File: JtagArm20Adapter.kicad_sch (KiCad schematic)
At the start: 7 parts, among them J1 Conn_02x03_Odd_Even, J2 Conn_01x05, J3 Conn_01x03, J4 Conn_02x10_Odd_Even, J5 B3B-PH-SM4-TB_LF__SN_

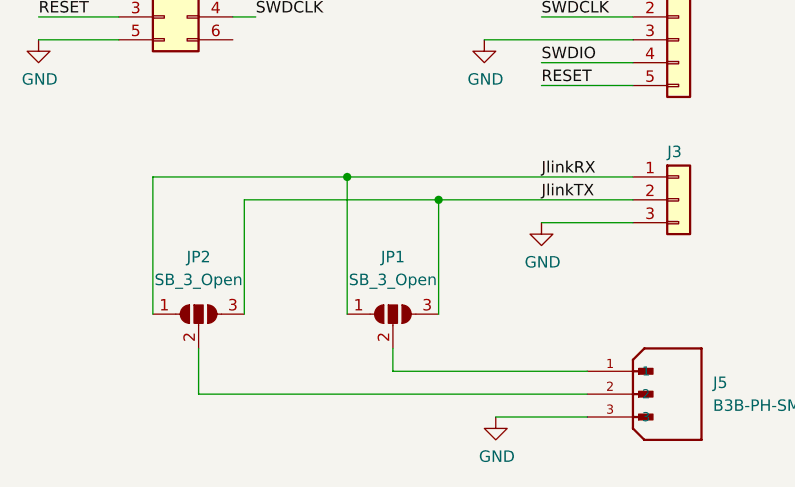
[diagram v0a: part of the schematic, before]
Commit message: moving solder bridges to top layer
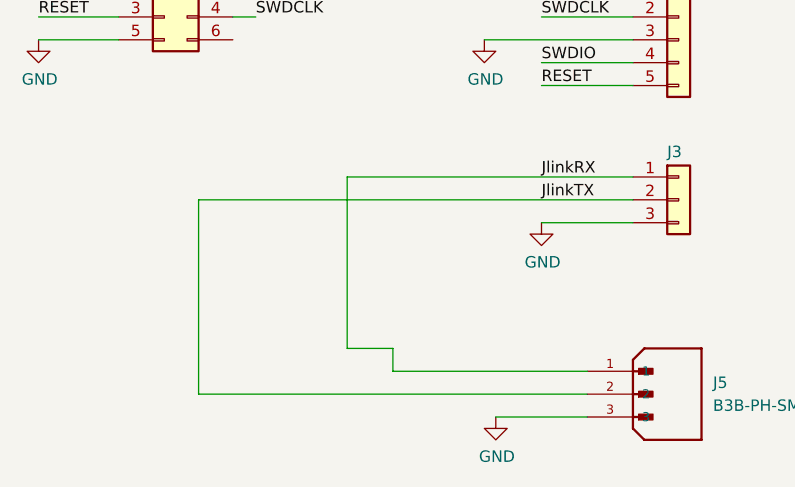
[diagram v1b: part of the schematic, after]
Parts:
- removed JP1, JP2: SB_3_Open, Jumper:SolderJumper-3_P1.3mm_Open_RoundedPad1.0x1.5mm, symbol Jumper:SolderJumper_3_Open
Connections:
- net JlinkRX: now also J5.1
- net JlinkTX: now also J5.2
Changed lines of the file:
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@@
-	)
-	(junction
-		(at 134.62 86.36)
-		(diameter 0)
-		(color 0 0 0 0)
 	)
 	(junction
@@
 	)
 	(junction
-		(at 124.46 83.82)
-		(diameter 0)
-		(color 0 0 0 0)
-	)
-	(junction
 		(at 237.49 71.12)
 		(diameter 0)
@@
 	(wire
 		(pts
-			(xy 134.62 99.06) (xy 134.62 86.36)
+			(xy 107.95 86.36) (xy 156.21 86.36)
 		)
 		(stroke
@@
 	(wire
 		(pts
-			(xy 102.87 99.06) (xy 102.87 83.82)
-		)
-		(stroke
-			(width 0)
-			(type default)
-		)
-	)
-	(wire
-		(pts
-			(xy 102.87 83.82) (xy 124.46 83.82)
-		)
-		(stroke
-			(width 0)
-			(type default)
-		)
-	)
-	(wire
-		(pts
 			(xy 237.49 71.12) (xy 237.49 83.82)
 		)
@@
 	(wire
 		(pts
-			(xy 107.95 102.87) (xy 107.95 107.95)
-		)
-		(stroke
-			(width 0)
-			(type default)
-		)
-	)
-	(wire
-		(pts
 			(xy 196.85 58.42) (xy 213.36 58.42)
 		)
@@
 	(wire
 		(pts
+			(xy 107.95 86.36) (xy 107.95 107.95)
+		)
+		(stroke
+			(width 0)
+			(type default)
+		)
+	)
+	(wire
+		(pts
 			(xy 146.05 71.12) (xy 156.21 71.12)
 		)
@@
 	(wire
 		(pts
-			(xy 124.46 99.06) (xy 124.46 83.82)
-		)
-		(stroke
-			(width 0)
-			(type default)
-		)
-	)
-	(wire
-		(pts
 			(xy 146.05 73.66) (xy 156.21 73.66)
 		)
@@
 	(wire
 		(pts
+			(xy 124.46 83.82) (xy 124.46 102.87)
+		)
+		(stroke
+			(width 0)
+			(type default)
+		)
+	)
+	(wire
+		(pts
 			(xy 111.76 66.04) (xy 114.3 66.04)
 		)
@@
 	(wire
 		(pts
+			(xy 124.46 102.87) (xy 129.54 102.87)
+		)
+		(stroke
+			(width 0)
+			(type default)
+		)
+	)
+	(wire
+		(pts
 			(xy 90.17 66.04) (xy 99.06 66.04)
 		)
@@
 	(wire
 		(pts
-			(xy 113.03 99.06) (xy 113.03 86.36)
-		)
-		(stroke
-			(width 0)
-			(type default)
-		)
-	)
-	(wire
-		(pts
 			(xy 237.49 63.5) (xy 237.49 66.04)
 		)
@@
 	(wire
 		(pts
-			(xy 113.03 86.36) (xy 134.62 86.36)
-		)
-		(stroke
-			(width 0)
-			(type default)
-		)
-	)
-	(wire
-		(pts
 			(xy 196.85 63.5) (xy 213.36 63.5)
 		)
@@
 		(pts
 			(xy 196.85 66.04) (xy 213.36 66.04)
-		)
-		(stroke
-			(width 0)
-			(type default)
-		)
-	)
-	(wire
-		(pts
-			(xy 134.62 86.36) (xy 156.21 86.36)
 		)
 		(stroke
@@
 	)
 	(symbol
-		(lib_id "Jumper:SolderJumper_3_Open")
-		(at 107.95 99.06 0)
-		(unit 1)
-		(exclude_from_sim no)
-		(in_bom no)
-		(on_board yes)
-		(dnp no)
-		(fields_autoplaced yes)
-		(property "Reference" "JP2"
-			(at 107.95 92.71 0)
-			(effects
-				(font
-					(size 1.27 1.27)
-				)
-			)
-		)
-		(property "Value" "SB_3_Open"
-			(at 107.95 95.25 0)
-			(effects
-				(font
-					(size 1.27 1.27)
-				)
-			)
-		)
-		(property "Footprint" "Jumper:SolderJumper-3_P1.3mm_Open_RoundedPad1.0x1.5mm"
-			(at 107.95 99.06 0)
-			(effects
-				(font
-					(size 1.27 1.27)
-				)
-				(hide yes)
-			)
-		)
-		(property "Datasheet" "~"
-			(at 107.95 99.06 0)
-			(effects
-				(font
-					(size 1.27 1.27)
-				)
-				(hide yes)
-			)
-		)
-		(property "Description" "Solder Jumper, 3-pole, open"
-			(at 107.95 99.06 0)
-			(effects
-				(font
-					(size 1.27 1.27)
-				)
-				(hide yes)
-			)
-		)
-		(pin "1"
-		)
-		(pin "3"
-		)
-		(pin "2"
-		)
-		(instances
-			(project ""
-				(path "/6b7e8426-0b4e-4827-9174-160ced800282"
-					(reference "JP2")
-					(unit 1)
-				)
-			)
-		)
-	)
-	(symbol
 		(lib_id "Connector_Generic:Conn_01x05")
 		(at 161.29 68.58 0)
@@
 					(unit 1)
 				)
-			)
-		)
-	)
-	(symbol
-		(lib_id "Jumper:SolderJumper_3_Open")
-		(at 129.54 99.06 0)
-		(unit 1)
-		(exclude_from_sim no)
-		(in_bom no)
-		(on_board yes)
-		(dnp no)
-		(property "Reference" "JP1"
-			(at 129.54 92.71 0)
-			(effects
-				(font
-					(size 1.27 1.27)
-				)
-			)
-		)
-		(property "Value" "SB_3_Open"
-			(at 129.54 95.25 0)
-			(effects
-				(font
-					(size 1.27 1.27)
-				)
-			)
-		)
-		(property "Footprint" "Jumper:SolderJumper-3_P1.3mm_Open_RoundedPad1.0x1.5mm"
-			(at 129.54 99.06 0)
-			(effects
-				(font
-					(size 1.27 1.27)
-				)
-				(hide yes)
-			)
-		)
-		(property "Datasheet" "~"
-			(at 129.54 99.06 0)
-			(effects
-				(font
-					(size 1.27 1.27)
-				)
-				(hide yes)
-			)
-		)
-		(property "Description" "Solder Jumper, 3-pole, open"
-			(at 129.54 99.06 0)
-			(effects
-				(font
-					(size 1.27 1.27)
-				)
-				(hide yes)
-			)
-		)
-		(pin "3"
-		)
-		(pin "1"
-		)
-		(pin "2"
-		)
-		(instances
-			(project ""
-				(path "/6b7e8426-0b4e-4827-9174-160ced800282"
-					(reference "JP1")
-					(unit 1)
-				)
